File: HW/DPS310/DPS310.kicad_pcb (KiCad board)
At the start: 2 copper layers, 32.2 x 27.4 mm, 7 parts, among them J1 Screw_Terminal_01x05, U1 DPS310

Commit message: Last Revision
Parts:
- moved JP1 53.4 mm to (115.5, 82.6)
- moved U1 51.1 mm to (126.8, 83.7), turned to 90 degrees
- moved C1 49.9 mm to (123.9, 83.4), turned to 90 degrees
- moved R3 47.9 mm to (120.7, 83.4), turned to 90 degrees
- moved J1 46.9 mm to (121.7, 97.1), turned to 90 degrees
- moved R1 44.4 mm to (134.2, 83.4), turned to 90 degrees
- moved R2 42.9 mm to (130.6, 83.4), turned to 90 degrees

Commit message: update for SPI and I2C support
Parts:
- added R4: 10K, Capacitor_SMD:C_0805_2012Metric_Pad1.15x1.40mm_HandSolder, F.Cu at (132.2, 88.0)
- C1: value C_Small -> 0.1uF
- J1: value Screw_Terminal_01x05 -> Screw_Terminal_01x06; footprint Connector_PinHeader_2.54mm:PinHeader_1x05_P2.54mm_Vertical -> Connector_PinHeader_2.54mm:PinHeader_1x06_P2.54mm_Vertical
- JP1: footprint Connector_PinHeader_2.54mm:PinHeader_1x02_P2.54mm_Vertical -> Jumper:SolderJumper-2_P1.3mm_Open_TrianglePad1.0x1.5mm; moved to B.Cu
- moved J1 2.31 mm to (119.6, 96.2)
- moved JP1 1.69 mm to (114.0, 83.3)
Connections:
- net /SCL renamed /SCL_SCK
- net /SDA renamed /SDI_SDA
- J1 pad 5: /INT -> /SDO_ADR
- JP1 pad 1: /INT -> /SDO_ADR
- JP1 pad 2: Net-(JP1-Pad2) -> GND
- R3 pad 1: Net-(JP1-Pad2) -> VCC
- R3 pad 2: GND -> /SDO_ADR
- U1 pad 2: Net-(U1-Pad2) -> /CS
- U1 pad 5: /INT -> /SDO_ADR

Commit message: Last revision of PCB
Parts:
- added REF**: MountingHole_2.2mm_M2_ISO7380_Pad, MountingHole:MountingHole_2.2mm_M2_ISO7380_Pad, F.Cu at (136.9, 78.5)
- added REF**: MountingHole_2.2mm_M2_ISO7380_Pad, MountingHole:MountingHole_2.2mm_M2_ISO7380_Pad, F.Cu at (114.7, 78.5)
- added REF**: MountingHole_2.2mm_M2_ISO7380_Pad, MountingHole:MountingHole_2.2mm_M2_ISO7380_Pad, F.Cu at (114.6, 92.2)
- added REF**: MountingHole_2.2mm_M2_ISO7380_Pad, MountingHole:MountingHole_2.2mm_M2_ISO7380_Pad, F.Cu at (136.9, 92.2)
- moved JP1 12.2 mm to (126.1, 83.4)
- moved R4 11.2 mm to (121.8, 83.8), turned to 90 degrees
- moved R3 10.3 mm to (131.0, 83.7)
- moved R1 8.62 mm to (126.2, 80.1), turned to 180 degrees
- moved R2 7.85 mm to (123.9, 87.5), turned to 0 degrees
- moved C1 5.84 mm to (128.1, 87.5), turned to 0 degrees
- moved J1 2.93 mm to (119.4, 93.3)
- moved U1 0.59 mm to (126.2, 83.7)
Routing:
- net VCC: track 0.00 -> 63.4 mm, vias 0 -> 1
- net /CS: track 0.00 -> 33.3 mm
- net /SDI_SDA: track 0.00 -> 33.1 mm
- net /SCL_SCK: track 0.00 -> 25.8 mm
- net GND: track 0.00 -> 21.3 mm, vias 0 -> 3
- net /SDO_ADR: track 0.00 -> 21.1 mm, vias 0 -> 1
- added copper zone on B.Cu, net (none)
- added copper zone on F.Cu, net GND
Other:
- board size 32.2 x 27.4 mm -> 30.6 x 22.8 mm

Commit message: New Last  Revision
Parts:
- moved R1 5.69 mm to (120.8, 81.6), turned to 0 degrees
- moved R2 5.04 mm to (120.8, 83.6)
- moved C1 3.87 mm to (131.9, 87.5), turned to 90 degrees
- moved JP1 2.39 mm to (125.8, 85.8)
- moved U1 2.08 mm to (125.8, 85.8)
- moved R4 2.00 mm to (120.8, 85.5), turned to 0 degrees
- moved R3 0.99 mm to (131.9, 83.8)
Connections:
- R2 pad 2: /SCL_SCK -> /SDI_SDA
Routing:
- net VCC: track 63.4 -> 32.6 mm, vias 1 -> 2
- net /SDI_SDA: track 33.1 -> 17.0 mm
- net /CS: track 33.3 -> 18.7 mm
- net GND: track 21.3 -> 15.5 mm, vias 3 -> 1
- net /SCL_SCK: track 25.8 -> 23.7 mm
- net /SDO_ADR: track 21.1 -> 19.6 mm
- added copper zone on B.Cu, net GND
- removed copper zone on B.Cu, net (none)
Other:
- net class Default: trace_width 0.25 -> 0.3
- net class VCC added: clearance 0.2, trace_width 0.5, via_dia 0.8, via_drill 0.4

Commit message: Last Revision
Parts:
- moved C1 1.33 mm to (132.1, 86.2)
- moved R3 1.33 mm to (132.1, 82.4)
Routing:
- net GND: track 15.5 -> 18.4 mm
- net /SCL_SCK: track 23.7 -> 25.9 mm
- net VCC: track 32.6 -> 34.4 mm
- net /SDO_ADR: track 19.6 -> 21.0 mm
- net /CS: track 18.7 -> 19.4 mm
- net /SDI_SDA: track 17.0 -> 17.5 mm

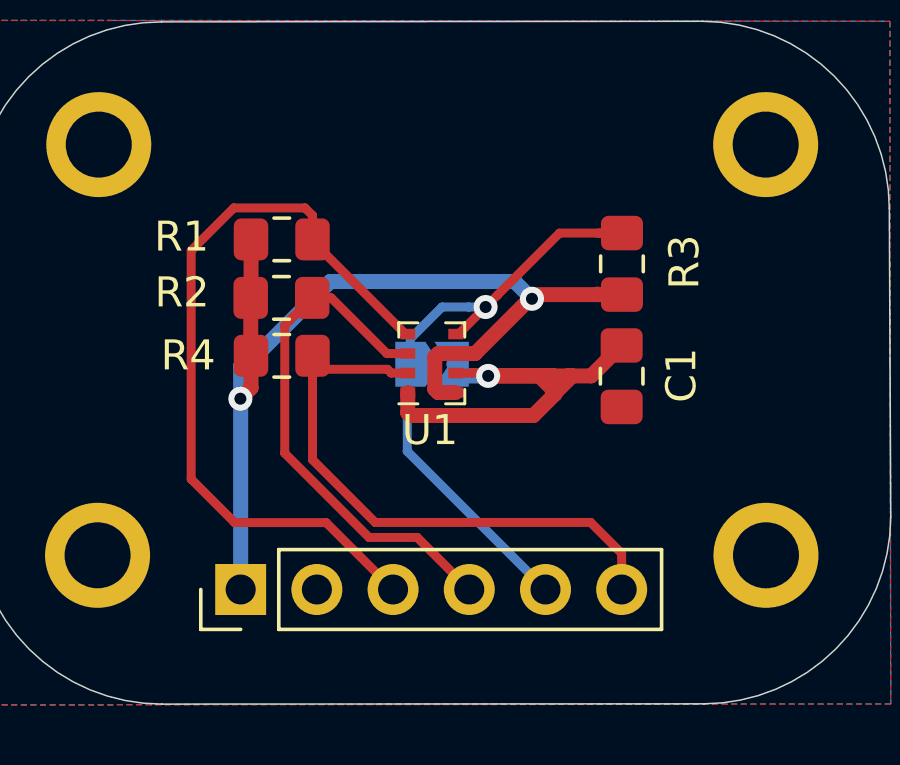
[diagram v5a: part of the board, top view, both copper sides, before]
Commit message: fix cap and traces
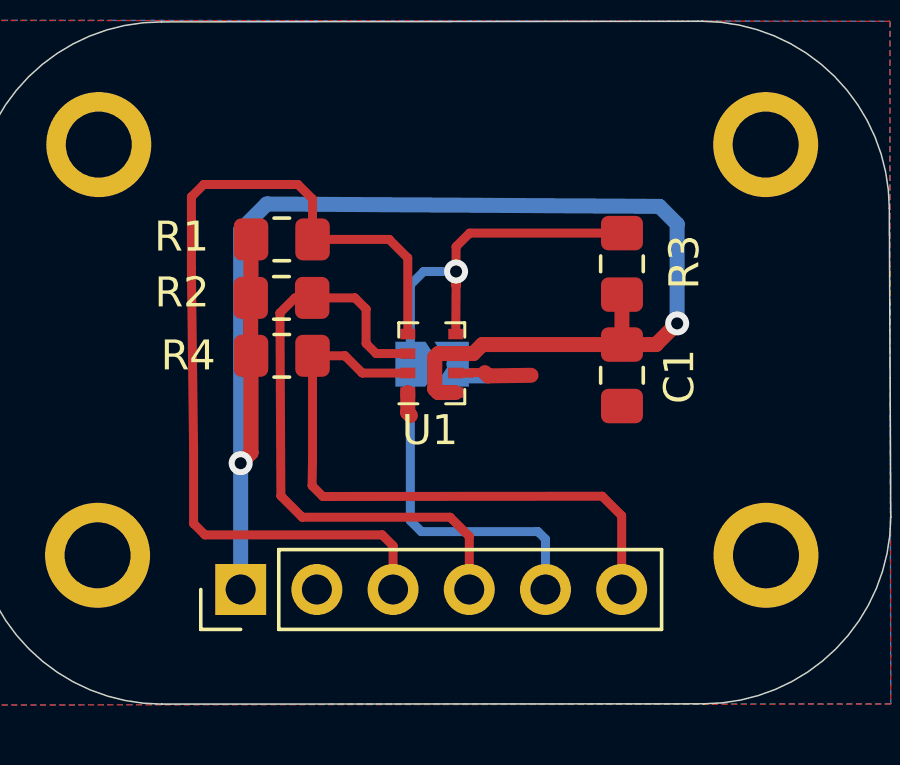
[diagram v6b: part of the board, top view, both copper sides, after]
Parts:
- turned C1 to 270 degrees
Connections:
- C1 pad 1: Net-(C1-Pad1) -> VCC
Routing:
- net VCC: track 34.4 -> 50.3 mm
- net GND: track 18.4 -> 4.67 mm, vias 1 -> 0
- net /SCL_SCK: track 25.9 -> 31.0 mm
- net /SDO_ADR: track 21.0 -> 25.1 mm
- net /SDI_SDA: track 17.5 -> 20.6 mm
- net /CS: track 19.4 -> 20.9 mm

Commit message: Update to KiCad 6.0
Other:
- net class Default removed
- net class VCC removed
